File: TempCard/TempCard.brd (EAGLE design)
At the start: 100 x 80 mm, 13 parts, among them Q1 MOSFET-NCHANNELBSS138, Q2 MOSFET-NCHANNELBSS138, U1 MIC5219 3.3V

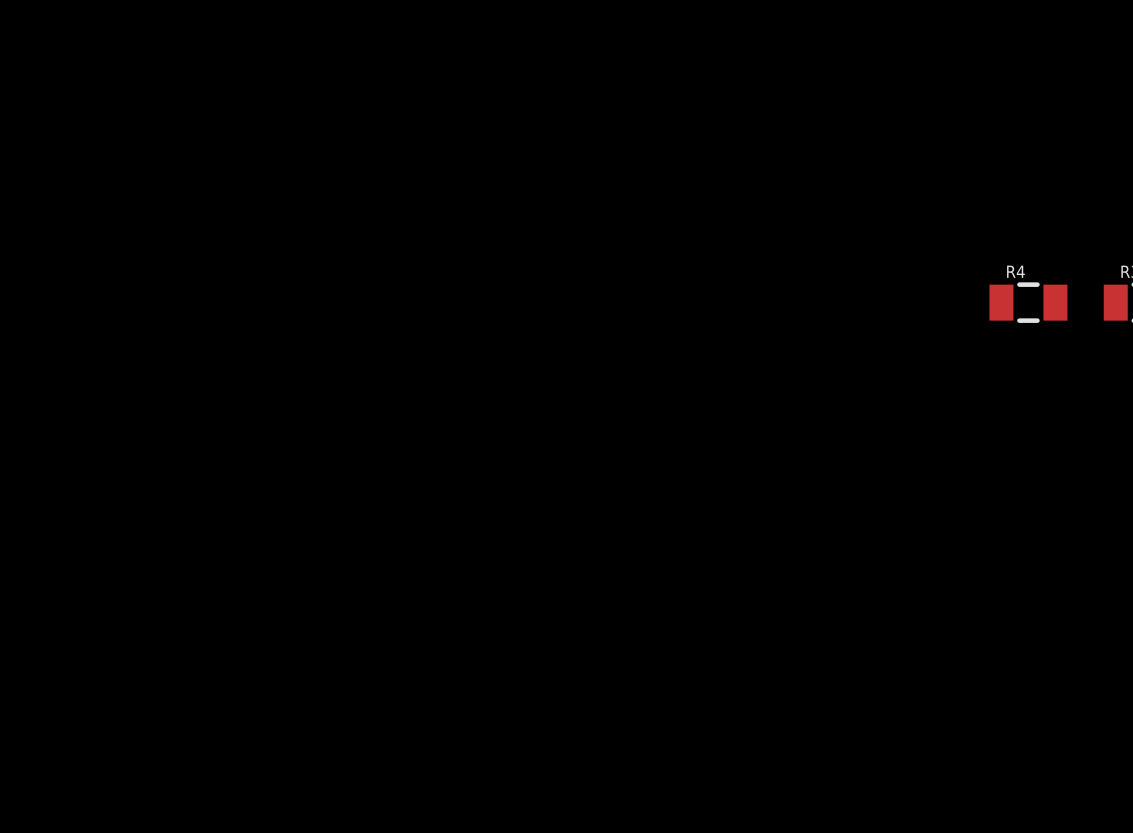
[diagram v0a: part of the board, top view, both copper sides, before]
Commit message: Adding sensors
BMP085, HMC5883L, SHT15

Signed-off-by: Scott Lerner <scottphiliplerner@gmail.com>
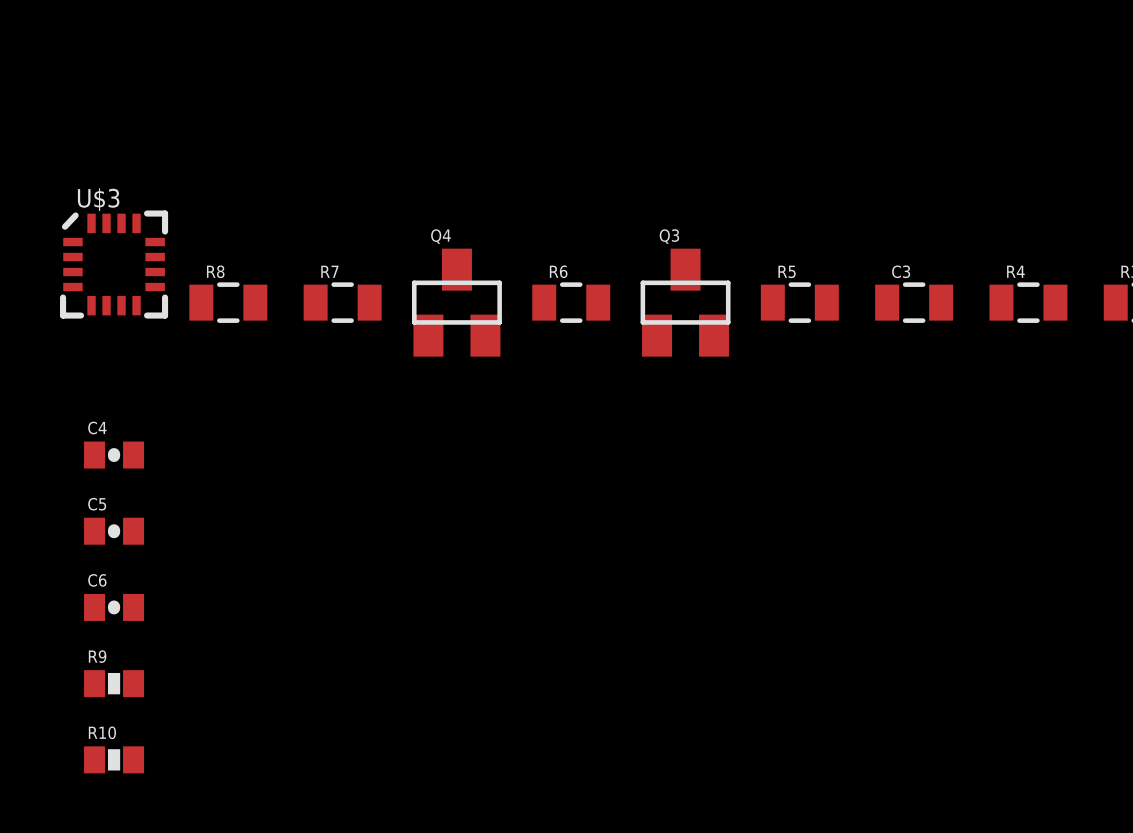
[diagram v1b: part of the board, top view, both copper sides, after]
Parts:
- added C3: 0.1uF, SparkFun-Capacitors:0805
- added C4: 4.7uF, SparkFun-Passives:0402-CAP
- added C5: 0.22uF, SparkFun-Passives:0402-CAP
- added C6: 0.1uF, SparkFun-Passives:0402-CAP
- added Q3, Q4: MOSFET-NCHANNELBSS138, SparkFun-DiscreteSemi:SOT23
- added R10, R9: DNP, SparkFun-Passives:0402-RES
- added R5, R6, R7, R8: (no value), SparkFun-Resistors:0805
- added U$3: HMC5883LSMD, SparkFun-Sensors:16LPCC
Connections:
- removed net VDD: U$2.4
- new net N$10: R9.1, U$3.1
- new net N$11: R10.1, U$3.16
- new net N$3: C4.1, U$3.10
- new net N$4: Q3.3, R6.1
- new net N$5: Q4.2, R7.1, U$2.3
- new net N$6: Q4.3, R8.1
- new net N$7: C5.1, U$3.8
- new net N$8: C5.2, U$3.12
- new net N$9: Q3.2, R5.1, U$2.2
- net 3.3V: now also C3.1, C6.1, Q3.1, Q4.1, R10.2, R5.2, R7.2, R9.2, U$2.4, U$3.13, U$3.2, U$3.4
- net 5V: now also R6.2, R8.2
- net GND: now also C3.2, C4.2, C6.2, U$3.11, U$3.9
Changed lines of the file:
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@@
 <element name="R3" library="SparkFun-Resistors" package="0805" value="" x="-41.91" y="-16.51"/>
 <element name="R4" library="SparkFun-Resistors" package="0805" value="" x="-45.72" y="-16.51"/>
+<element name="C3" library="SparkFun-Capacitors" package="0805" value="0.1uF" x="-49.53" y="-16.51">
+<attribute name="PROD_ID" value="CAP-11625" x="-49.53" y="-16.51" size="1.778" layer="27" ratio="15" display="off"/>
+</element>
+<element name="R5" library="SparkFun-Resistors" package="0805" value="" x="-53.34" y="-16.51"/>
+<element name="Q3" library="SparkFun-DiscreteSemi" package="SOT23" value="MOSFET-NCHANNELBSS138" x="-57.15" y="-16.51">
+<attribute name="PROD_ID" value="TRANS-00830" x="-57.15" y="-16.51" size="1.778" layer="27" ratio="15" display="off"/>
+</element>
+<element name="R6" library="SparkFun-Resistors" package="0805" value="" x="-60.96" y="-16.51"/>
+<element name="Q4" library="SparkFun-DiscreteSemi" package="SOT23" value="MOSFET-NCHANNELBSS138" x="-64.77" y="-16.51">
+<attribute name="PROD_ID" value="TRANS-00830" x="-64.77" y="-16.51" size="1.778" layer="27" ratio="15" display="off"/>
+</element>
+<element name="R7" library="SparkFun-Resistors" package="0805" value="" x="-68.58" y="-16.51"/>
+<element name="R8" library="SparkFun-Resistors" package="0805" value="" x="-72.39" y="-16.51"/>
+<element name="U$3" library="SparkFun-Sensors" package="16LPCC" value="HMC5883LSMD" x="-76.2" y="-15.24"/>
+<element name="C4" library="SparkFun-Passives" package="0402-CAP" value="4.7uF" x="-76.2" y="-21.59"/>
+<element name="C5" library="SparkFun-Passives" package="0402-CAP" value="0.22uF" x="-76.2" y="-24.13"/>
+<element name="C6" library="SparkFun-Passives" package="0402-CAP" value="0.1uF" x="-76.2" y="-26.67"/>
+<element name="R9" library="SparkFun-Passives" package="0402-RES" value="DNP" x="-76.2" y="-29.21"/>
+<element name="R10" library="SparkFun-Passives" package="0402-RES" value="DNP" x="-76.2" y="-31.75"/>
 </elements>
 <signals>
 <signal name="GND">
 <contactref element="U$1" pad="1"/>
-<contactref element="U$2" pad="1"/>
 <contactref element="U1" pad="2"/>
 <contactref element="C2" pad="2"/>
 <contactref element="C1" pad="2"/>
 <contactref element="U$1" pad="1"/>
-<wire x1="-29.58" y1="-16.51" x2="-26.67" y2="-17.8101" width="0" layer="19" extent="1-1"/>
+<contactref element="U$2" pad="1"/>
+<contactref element="C3" pad="2"/>
+<contactref element="C4" pad="2"/>
+<contactref element="U$3" pad="9"/>
+<contactref element="U$3" pad="11"/>
+<contactref element="C6" pad="2"/>
+<wire x1="-75.55" y1="-21.59" x2="-75.55" y2="-26.67" width="0" layer="19" extent="1-1"/>
+<wire x1="-74.83" y1="-15.99" x2="-75.55" y2="-21.59" width="0" layer="19" extent="1-1"/>
+<wire x1="-74.83" y1="-14.99" x2="-74.83" y2="-15.99" width="0" layer="19" extent="1-1"/>
+<wire x1="-48.63" y1="-16.51" x2="-74.83" y2="-15.99" width="0" layer="19" extent="1-1"/>
+<wire x1="-29.58" y1="-16.51" x2="-48.63" y2="-16.51" width="0" layer="19" extent="1-1"/>
+<wire x1="-26.67" y1="-17.8101" x2="-29.58" y2="-16.51" width="0" layer="19" extent="1-1"/>
 <wire x1="-14.34" y1="-16.51" x2="-26.67" y2="-17.8101" width="0" layer="19" extent="1-1"/>
 <wire x1="-11.557" y1="-13.335" x2="-14.34" y2="-16.51" width="0" layer="19" extent="1-1"/>
 <wire x1="1.745" y1="-15.24" x2="-11.557" y2="-13.335" width="0" layer="19" extent="1-1"/>
-</signal>
-<signal name="VDD">
-<contactref element="U$2" pad="4"/>
 </signal>
 <signal name="5V">
@@
 <contactref element="R2" pad="2"/>
 <contactref element="R4" pad="2"/>
+<contactref element="R6" pad="2"/>
+<contactref element="R8" pad="2"/>
+<wire x1="-60.06" y1="-16.51" x2="-71.49" y2="-16.51" width="0" layer="19" extent="1-1"/>
+<wire x1="-44.82" y1="-16.51" x2="-60.06" y2="-16.51" width="0" layer="19" extent="1-1"/>
 <wire x1="-33.39" y1="-16.51" x2="-44.82" y2="-16.51" width="0" layer="19" extent="1-1"/>
 <wire x1="-31.38" y1="-16.51" x2="-33.39" y2="-16.51" width="0" layer="19" extent="1-1"/>
@@
 <contactref element="R3" pad="2"/>
 <contactref element="Q2" pad="1"/>
+<contactref element="R5" pad="2"/>
+<contactref element="Q3" pad="1"/>
+<contactref element="R7" pad="2"/>
+<contactref element="Q4" pad="1"/>
+<contactref element="U$2" pad="4"/>
+<contactref element="C3" pad="1"/>
+<contactref element="U$3" pad="4"/>
+<contactref element="U$3" pad="13"/>
+<contactref element="U$3" pad="2"/>
+<contactref element="R9" pad="2"/>
+<contactref element="R10" pad="2"/>
+<contactref element="C6" pad="1"/>
+<wire x1="-75.55" y1="-29.21" x2="-75.55" y2="-31.75" width="0" layer="19" extent="1-1"/>
+<wire x1="-76.85" y1="-26.67" x2="-75.55" y2="-29.21" width="0" layer="19" extent="1-1"/>
+<wire x1="-77.57" y1="-15.99" x2="-76.85" y2="-26.67" width="0" layer="19" extent="1-1"/>
+<wire x1="-77.57" y1="-14.99" x2="-77.57" y2="-15.99" width="0" layer="19" extent="1-1"/>
+<wire x1="-75.45" y1="-13.87" x2="-77.57" y2="-14.99" width="0" layer="19" extent="1-1"/>
+<wire x1="-67.68" y1="-16.51" x2="-75.45" y2="-13.87" width="0" layer="19" extent="1-1"/>
+<wire x1="-65.72" y1="-17.61" x2="-67.68" y2="-16.51" width="0" layer="19" extent="1-1"/>
+<wire x1="-58.1" y1="-17.61" x2="-65.72" y2="-17.61" width="0" layer="19" extent="1-1"/>
+<wire x1="-52.44" y1="-16.51" x2="-58.1" y2="-17.61" width="0" layer="19" extent="1-1"/>
+<wire x1="-50.43" y1="-16.51" x2="-52.44" y2="-16.51" width="0" layer="19" extent="1-1"/>
+<wire x1="-41.01" y1="-16.51" x2="-50.43" y2="-16.51" width="0" layer="19" extent="1-1"/>
 <wire x1="-39.05" y1="-17.61" x2="-41.01" y2="-16.51" width="0" layer="19" extent="1-1"/>
 <wire x1="-27.62" y1="-15.2099" x2="-39.05" y2="-17.61" width="0" layer="19" extent="1-1"/>
@@
 <wire x1="-18.15" y1="-16.51" x2="-23.81" y2="-17.61" width="0" layer="19" extent="1-1"/>
 <wire x1="-16.14" y1="-16.51" x2="-18.15" y2="-16.51" width="0" layer="19" extent="1-1"/>
-<wire x1="1.745" y1="-17.78" x2="-16.14" y2="-16.51" width="0" layer="19" extent="1-1"/>
+<wire x1="-11.557" y1="-17.145" x2="-16.14" y2="-16.51" width="0" layer="19" extent="1-1"/>
+<wire x1="1.745" y1="-17.78" x2="-11.557" y2="-17.145" width="0" layer="19" extent="1-1"/>
 <wire x1="3.81" y1="-18.575" x2="1.745" y2="-17.78" width="0" layer="19" extent="1-1"/>
 </signal>
@@
 <wire x1="-38.1" y1="-15.41" x2="-46.62" y2="-16.51" width="0" layer="19" extent="1-1"/>
 </signal>
+<signal name="N$4">
+<contactref element="Q3" pad="3"/>
+<contactref element="R6" pad="1"/>
+<wire x1="-57.15" y1="-15.41" x2="-61.86" y2="-16.51" width="0" layer="19" extent="1-1"/>
+</signal>
+<signal name="N$5">
+<contactref element="R7" pad="1"/>
+<contactref element="Q4" pad="2"/>
+<contactref element="U$2" pad="3"/>
+<wire x1="-63.82" y1="-17.61" x2="-69.48" y2="-16.51" width="0" layer="19" extent="1-1"/>
+<wire x1="-11.557" y1="-15.875" x2="-63.82" y2="-17.61" width="0" layer="19" extent="1-1"/>
+</signal>
+<signal name="N$6">
+<contactref element="Q4" pad="3"/>
+<contactref element="R8" pad="1"/>
+<wire x1="-64.77" y1="-15.41" x2="-73.29" y2="-16.51" width="0" layer="19" extent="1-1"/>
+</signal>
+<signal name="N$9">
+<contactref element="U$2" pad="2"/>
+<contactref element="R5" pad="1"/>
+<contactref element="Q3" pad="2"/>
+<wire x1="-54.24" y1="-16.51" x2="-56.2" y2="-17.61" width="0" layer="19" extent="1-1"/>
+<wire x1="-11.557" y1="-14.605" x2="-54.24" y2="-16.51" width="0" layer="19" extent="1-1"/>
+</signal>
+<signal name="N$3">
+<contactref element="U$3" pad="10"/>
+<contactref element="C4" pad="1"/>
+<wire x1="-74.83" y1="-15.49" x2="-76.85" y2="-21.59" width="0" layer="19" extent="1-1"/>
+</signal>
+<signal name="N$7">
+<contactref element="U$3" pad="8"/>
+<contactref element="C5" pad="1"/>
+<wire x1="-75.45" y1="-16.61" x2="-76.85" y2="-24.13" width="0" layer="19" extent="1-1"/>
+</signal>
+<signal name="N$8">
+<contactref element="U$3" pad="12"/>
+<contactref element="C5" pad="2"/>
+<wire x1="-74.83" y1="-14.49" x2="-75.55" y2="-24.13" width="0" layer="19" extent="1-1"/>
+</signal>
+<signal name="N$11">
+<contactref element="U$3" pad="16"/>
+<contactref element="R10" pad="1"/>
+<wire x1="-76.95" y1="-13.87" x2="-76.85" y2="-31.75" width="0" layer="19" extent="1-1"/>
+</signal>
+<signal name="N$10">
+<contactref element="U$3" pad="1"/>
+<contactref element="R9" pad="1"/>
+<wire x1="-77.57" y1="-14.49" x2="-76.85" y2="-29.21" width="0" layer="19" extent="1-1"/>
+</signal>
 </signals>
